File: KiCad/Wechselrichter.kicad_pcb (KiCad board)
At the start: 2 copper layers, 73.7 x 33 mm, 40 parts, among them J1 Conn_01x01_Pin, J2 Conn_01x01_Pin, J3 Conn_01x01_Pin, J4 Conn_01x01_Pin, J5 Conn_01x01_Pin, J6 Conn_01x01_Pin, Q1 2N3904, Q10 IRF540N, Q2 2N3904, Q3 2N3904, Q4 2N3904, Q5 SS8050, Q6 SS8550, Q7 SS8050, Q8 SS8550, Q9 IRF540N

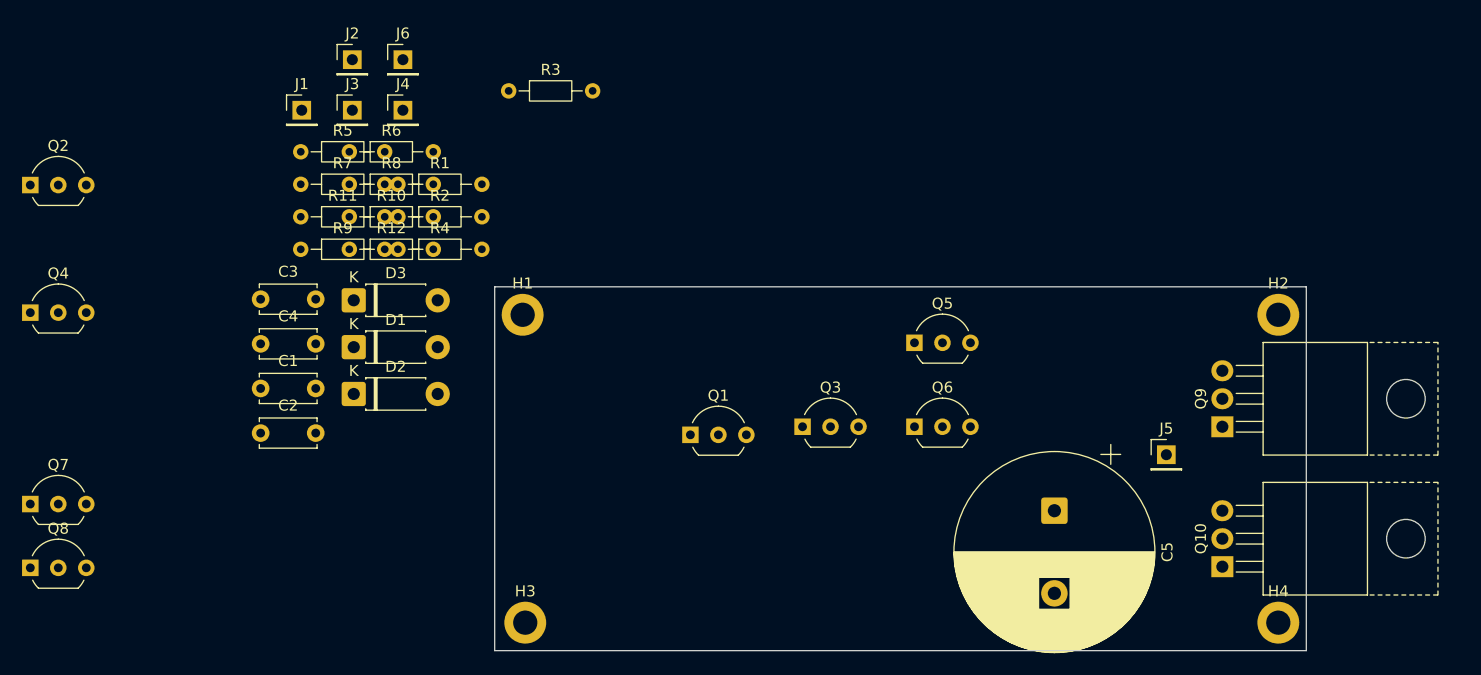
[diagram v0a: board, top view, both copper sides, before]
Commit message: Komponentenplatzierung. RC-Glied und Elko wegen Platzmangel auf PCB weggelassen.
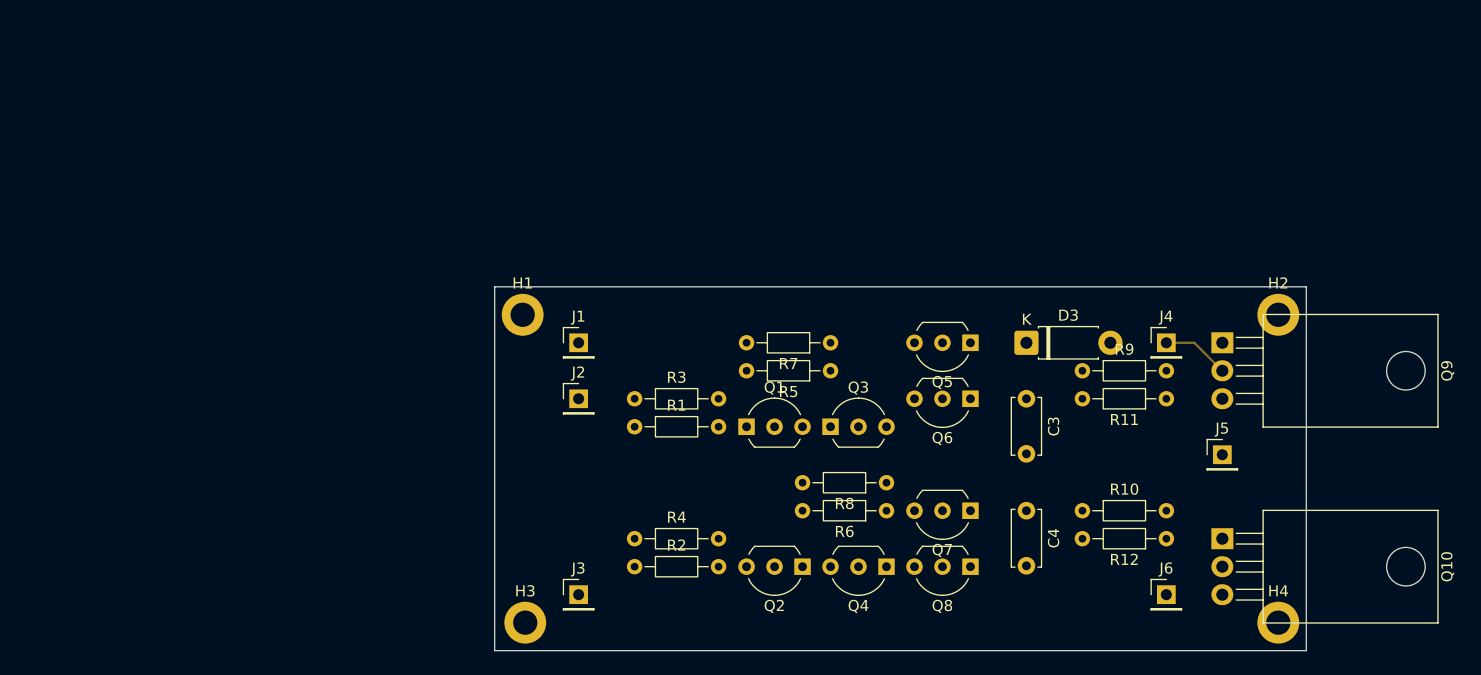
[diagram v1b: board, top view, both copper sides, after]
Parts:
- removed C1, C2: 1n/50V, Capacitor_THT:C_Disc_D5.0mm_W2.5mm_P5.00mm
- removed C5: 68uF, Capacitor_THT:CP_Radial_D18.0mm_P7.50mm
- removed D1, D2: 1N4007, Diode_THT:D_DO-41_SOD81_P7.62mm_Horizontal
- Q10, Q9: footprint Package_TO_SOT_THT:TO-220-3_Horizontal_TabUp -> Package_TO_SOT_THT:TO-220-3_Horizontal_TabDown
- moved Q7 85.3 mm to (162.6, 81.3), turned to 180 degrees
- moved Q8 85.3 mm to (162.6, 86.4), turned to 180 degrees
- moved J6 84.6 mm to (180.3, 88.9)
- moved Q4 81.1 mm to (154.9, 86.4), turned to 180 degrees
- moved R11 80.3 mm to (180.3, 71.1), turned to 180 degrees
- moved R12 78.7 mm to (180.3, 83.8), turned to 180 degrees
- moved Q2 78.2 mm to (147.3, 86.4), turned to 180 degrees
- moved J4 72.4 mm to (180.3, 66.0)
- moved R9 71.8 mm to (172.7, 68.6)
- moved R10 71.7 mm to (172.7, 81.3)
- moved C4 71.1 mm to (167.6, 81.3), turned to -90 degrees
- moved C3 70.1 mm to (167.6, 71.1), turned to -90 degrees
- moved D3 61.2 mm to (167.6, 66.0)
- moved R6 58.6 mm to (154.9, 81.3), turned to 180 degrees
- moved R8 55.8 mm to (154.9, 78.7), turned to 180 degrees
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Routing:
- net GND: track 0.00 -> 59.8 mm
- net +18V: track 0.00 -> 6.13 mm
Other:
- copper layers 2 -> 10

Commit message: Platzierung und Routing. RC-Glied wieder untergekriegt.
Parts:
- added C5: 1n/50V, Capacitor_THT:C_Disc_D5.0mm_W2.5mm_P5.00mm, F.Cu at (139.7, 73.7)
- added C6: 1n/50V, Capacitor_THT:C_Disc_D5.0mm_W2.5mm_P5.00mm, F.Cu at (139.7, 83.8)
- added D4: 1N4007, Diode_THT:D_DO-41_SOD81_P7.62mm_Horizontal, F.Cu at (129.5, 66.0)
- added D5: 1N4007, Diode_THT:D_DO-41_SOD81_P7.62mm_Horizontal, F.Cu at (129.5, 81.3)
- moved Q5 5.08 mm to (157.5, 66.0), turned to 0 degrees
- moved Q6 5.08 mm to (157.5, 71.1), turned to 0 degrees
- moved Q7 5.08 mm to (157.5, 81.3), turned to 0 degrees
- moved Q8 5.08 mm to (157.5, 86.4), turned to 0 degrees
- moved J2 5.08 mm to (127.0, 76.2)
- moved Q2 3.59 mm to (144.8, 83.8), turned to -90 degrees
- moved Q4 3.59 mm to (152.4, 83.8), turned to -90 degrees
- moved Q1 3.59 mm to (144.8, 71.1), turned to -90 degrees
- moved Q3 3.59 mm to (152.4, 71.1), turned to -90 degrees
- moved R1 2.54 mm to (129.5, 73.7)
- moved R2 2.54 mm to (129.5, 86.4)
- moved R3 2.54 mm to (129.5, 71.1)
- moved R4 2.54 mm to (129.5, 83.8)
- moved C3 2.54 mm to (167.6, 68.6)
- moved C4 2.54 mm to (167.6, 78.7)
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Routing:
- net GND: track 59.8 -> 118.4 mm
- net Net-(J5-Pin_1): track 0.00 -> 50.3 mm
- net +18V: track 6.13 -> 55.4 mm
- net Net-(D3-K): track 0.00 -> 25.4 mm
- net Net-(Q4-C): track 0.00 -> 23.5 mm
- net Net-(Q3-C): track 0.00 -> 23.3 mm
- net Net-(Q5-E): track 0.00 -> 16.3 mm
- net Net-(D4-A): track 0.00 -> 16.3 mm
- net Net-(Q7-E): track 0.00 -> 15.2 mm
- net Net-(Q1-C): track 0.00 -> 11.2 mm
- net Net-(D5-A): track 0.00 -> 11.2 mm
- net Net-(D5-K): track 0.00 -> 11.2 mm
- net Net-(Q2-C): track 0.00 -> 10.9 mm
- net Net-(D4-K): track 0.00 -> 9.72 mm
- net Net-(Q9-G): track 0.00 -> 7.62 mm
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
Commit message: QSpice: Widerstände in der "h_bridge" Simulation angepasst. Werte in KiCAD übertragen. Richtige BJT-Symblos gewählt.
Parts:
- removed Q3, Q4: 2N3904, Package_TO_SOT_THT:TO-92_Inline_Wide
- removed Q5, Q7: SS8050, Package_TO_SOT_THT:TO-92_Inline_Wide
- removed Q6, Q8: SS8550, Package_TO_SOT_THT:TO-92_Inline_Wide
- added Q12: 2N3904, Package_TO_SOT_THT:TO-92L_Inline_Wide, F.Cu at (152.4, 76.2)
- added Q13: 2N3904, Package_TO_SOT_THT:TO-92L_Inline_Wide, F.Cu at (144.8, 76.2)
- added Q14: SS8050, Package_TO_SOT_THT:TO-92L_Inline_Wide, F.Cu at (162.6, 66.0)
- added Q15: 2N3904, Package_TO_SOT_THT:TO-92L_Inline_Wide, F.Cu at (144.8, 88.9)
- added Q16: 2N3904, Package_TO_SOT_THT:TO-92L_Inline_Wide, F.Cu at (152.4, 88.9)
- added Q17: SS8050, Package_TO_SOT_THT:TO-92L_Inline_Wide, F.Cu at (162.6, 81.3)
- Q1, Q2: value 2N3904 -> SS8550; footprint Package_TO_SOT_THT:TO-92_Inline_Wide -> Package_TO_SOT_THT:TO-92L_Inline_Wide
- Q10, Q9: footprint Package_TO_SOT_THT:TO-220-3_Horizontal_TabDown -> Package_TO_SOT_THT:TO-220-3_Horizontal_TabUp; moved to B.Cu
- R1, R2: value 10k -> 5k1
- R11, R12: value 10k -> 100k
- moved Q2 18.0 mm to (162.6, 86.4), turned to 180 degrees
- moved Q1 17.8 mm to (162.6, 71.1), turned to 180 degrees
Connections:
- Q1 pad 1: Net-(Q1-C) -> Net-(Q1-E)
- Q1 pad 2: Net-(D4-A) -> Net-(Q1-B)
- Q1 pad 3: GND -> Net-(J5-Pin_1)
- Q2 pad 1: Net-(Q2-C) -> Net-(Q17-E)
- Q2 pad 2: Net-(D5-A) -> Net-(Q16-C)
- R10 pad 1: Net-(Q7-E) -> Net-(Q17-E)
- R5 pad 2: Net-(Q1-C) -> Net-(Q12-B)
- R6 pad 2: Net-(Q2-C) -> Net-(Q15-C)
- R7 pad 2: Net-(Q3-C) -> Net-(Q1-B)
- R8 pad 2: Net-(Q4-C) -> Net-(Q16-C)
- R9 pad 1: Net-(Q5-E) -> Net-(Q1-E)
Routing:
- net Net-(Q4-C): track 23.5 -> 0.00 mm
- net Net-(Q16-C): track 0.00 -> 23.5 mm
- net Net-(Q3-C): track 23.3 -> 0.00 mm
- net Net-(Q1-B): track 0.00 -> 23.3 mm
- net Net-(Q5-E): track 16.3 -> 0.00 mm
- net Net-(Q1-E): track 0.00 -> 16.3 mm
- net Net-(Q7-E): track 15.2 -> 0.00 mm
- net Net-(Q17-E): track 0.00 -> 15.2 mm
- net Net-(Q12-B): track 0.00 -> 11.2 mm
- net Net-(Q1-C): track 11.2 -> 0.00 mm
- net Net-(Q2-C): track 10.9 -> 0.00 mm
- net Net-(Q15-C): track 0.00 -> 10.9 mm
- net Net-(J5-Pin_1): track 50.3 -> 44.8 mm
- net Net-(D4-A): track 16.3 -> 13.8 mm

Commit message: Diode in RC-Glied weggelassen. Lediglich 22pF zur leichten Glättung ung Entkopplung.
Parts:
- C5, C6: value 1n/50V -> 22p/50V
- moved J2 7.62 mm to (127.0, 83.8)
- moved J1 2.54 mm to (127.0, 71.1)
- moved C5 2.54 mm to (139.7, 71.1)
- moved J4 2.54 mm to (182.9, 66.0)
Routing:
- net Net-(D5-K): track 11.2 -> 7.62 mm
- net Net-(J5-Pin_1): track 44.8 -> 46.8 mm
- net Net-(D5-A): track 11.2 -> 12.7 mm
- net +18V: track 55.4 -> 56.9 mm
- net Net-(Q16-C): track 23.5 -> 22.4 mm
- net GND: track 118.4 -> 119.4 mm
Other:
- board text added: "01"
- board text added: "02"
- board text added: "03"
- board text added: "04"
- board text added: "05"
- board text added: "06"
- board text added: "07"
- board text added: "08"
- board text added: "09"
- board text added: "10"
- board text added: "A"
- board text added: "B"
- board text added: "C"
- board text added: "D"
- board text added: "E"
- board text added: "F"
- board text added: "G"
- board text added: "H"
- board text added: "I"
- board text added: "J"
- board text added: "K"
- board text added: "L"
- board text added: "M"
- board text added: "N"
- board text added: "O"
- board text added: "P"
- board text added: "Q"
- board text added: "R"
- board text added: "S"
- board text added: "T"
- board text added: "U"
- board text added: "V"
- board text added: "W"
- board text added: "X"
